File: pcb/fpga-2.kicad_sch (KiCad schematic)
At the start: 1 part, among them U5 XC7A100T-FGG484

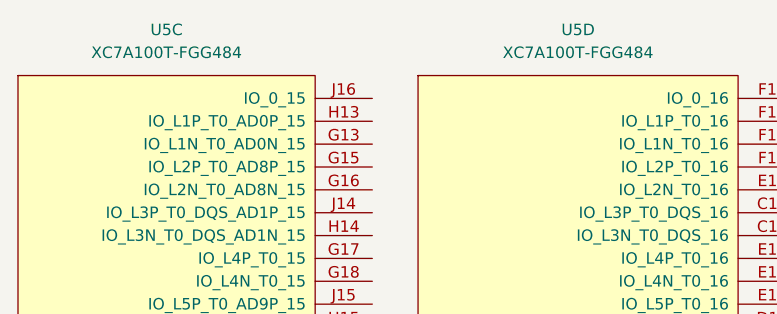
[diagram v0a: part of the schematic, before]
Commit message: moved stuff around, bom
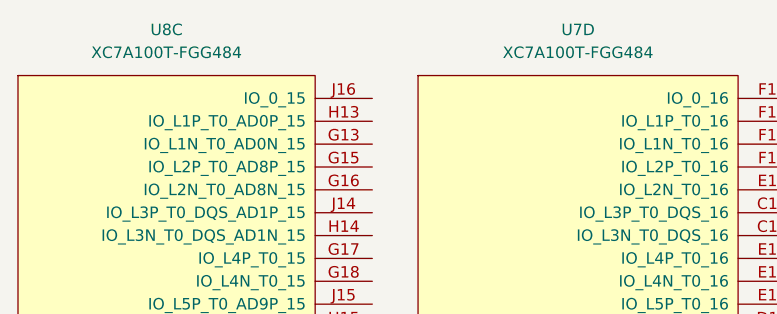
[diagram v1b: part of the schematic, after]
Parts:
- renumbered U5 to U7, U5 to U8
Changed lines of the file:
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@@
 		(dnp no)
 		(fields_autoplaced yes)
-		(property "Reference" "U5"
+		(property "Reference" "U7"
 			(at 99.06 25.4 0)
 			(effects
@@
 			(project "RPi-HwAB-1"
 				(path "/e63e39d7-6ac0-4ffd-8aa3-1841a4541b55/59d21473-a004-4514-8090-fd93db818925/ef42fd34-c1d8-421f-b8cb-1078e483aec9"
-					(reference "U5")
+					(reference "U7")
 					(unit 4)
 				)
@@
 		(dnp no)
 		(fields_autoplaced yes)
-		(property "Reference" "U5"
+		(property "Reference" "U8"
 			(at 53.34 25.4 0)
 			(effects
@@
 			(project "RPi-HwAB-1"
 				(path "/e63e39d7-6ac0-4ffd-8aa3-1841a4541b55/59d21473-a004-4514-8090-fd93db818925/ef42fd34-c1d8-421f-b8cb-1078e483aec9"
-					(reference "U5")
+					(reference "U8")
 					(unit 3)
 				)

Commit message: decoupling
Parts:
- added C129, C135, C136, C137, C138, C139, C140, C141, C142, C143, C144, C145: 0.1uF, Capacitor_SMD:C_0402_1005Metric, symbol library:C
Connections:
- net 3V3_FD: now reaches U7.A17 (VCCO_16)
- net 3V3_FD: now also U7.B14 (VCCO_16), U7.C21 (VCCO_16), U7.D18 (VCCO_16), U7.E15 (VCCO_16), U7.F22 (VCCO_16), U8.G19 (VCCO_15), U8.H16 (VCCO_15), U8.J13 (VCCO_15), U8.K20 (VCCO_15), U8.L17 (VCCO_15), U8.N21 (VCCO_15), C129.2, C135.2, C136.2, C137.2, C138.2, C139.2, C140.2, C141.2, C142.2, C143.2, C144.2, C145.2
- new net GND: C129.1, C135.1, C136.1, C137.1, C138.1, C139.1, C140.1, C141.1, C142.1, C143.1, C144.1, C145.1
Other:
- moved on the sheet: U7D, U8C

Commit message: bom
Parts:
- C30: renamed from C129; Part Description (none) -> CAP CER 0.1UF 16V X7R 0402
- C31: renamed from C140; Part Description (none) -> CAP CER 0.1UF 16V X7R 0402
- C32: renamed from C135; Part Description (none) -> CAP CER 0.1UF 16V X7R 0402
- C33: renamed from C141; Part Description (none) -> CAP CER 0.1UF 16V X7R 0402
- C34: renamed from C136; Part Description (none) -> CAP CER 0.1UF 16V X7R 0402
- C35: renamed from C142; Part Description (none) -> CAP CER 0.1UF 16V X7R 0402
- C36: renamed from C137; Part Description (none) -> CAP CER 0.1UF 16V X7R 0402
- C37: renamed from C143; Part Description (none) -> CAP CER 0.1UF 16V X7R 0402
- C38: renamed from C138; Part Description (none) -> CAP CER 0.1UF 16V X7R 0402
- C39: renamed from C144; Part Description (none) -> CAP CER 0.1UF 16V X7R 0402
- C40: renamed from C139; Part Description (none) -> CAP CER 0.1UF 16V X7R 0402
- C41: renamed from C145; Part Description (none) -> CAP CER 0.1UF 16V X7R 0402
- U7: Manufacturer (none) -> AMD; Manufacturer Product Number (none) -> XC7A100T-1FGG484C; Part Description (none) -> IC FPGA 285 I/O 484FBGA
- U7: renamed from U8; Manufacturer (none) -> AMD; Manufacturer Product Number (none) -> XC7A100T-1FGG484C; Part Description (none) -> IC FPGA 285 I/O 484FBGA
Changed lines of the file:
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@@
 		(on_board yes)
 		(dnp no)
-		(property "Reference" "C140"
+		(property "Reference" "C31"
 			(at 217.17 123.19 0)
 			(effects
@@
 			)
 		)
+		(property "Part Description" "CAP CER 0.1UF 16V X7R 0402"
+			(at 215.9 125.73 0)
+			(effects
+				(font
+					(size 1.27 1.27)
+				)
+				(hide yes)
+			)
+		)
 		(pin "1"
 		)
@@
 			(project "RPi-HwAB-1"
 				(path "/e63e39d7-6ac0-4ffd-8aa3-1841a4541b55/59d21473-a004-4514-8090-fd93db818925/ef42fd34-c1d8-421f-b8cb-1078e483aec9"
-					(reference "C140")
+					(reference "C31")
 					(unit 1)
 				)
@@
 			)
 		)
-		(property "Datasheet" ""
+		(property "Datasheet" "https://docs.amd.com/search/all?value-filters=Document_Type_custom~%2522Data+Sheet%2522_%2522Introductory+Resources%257CSelection+Guide%2522_%2522Introductory+Resources%257CWhite+Paper%2522*Product_custom~%2522Adaptive+SoCs+%2526+FPGAs%257CFPGA%257CArtix+7%2522&content-lang=en-US"
 			(at 144.78 76.2 0)
 			(effects
@@
 					(size 1.27 1.27)
 				)
+				(hide yes)
 			)
 		)
@@
 			)
 		)
+		(property "Manufacturer" "AMD"
+			(at 144.78 76.2 0)
+			(effects
+				(font
+					(size 1.27 1.27)
+				)
+				(hide yes)
+			)
+		)
+		(property "Manufacturer Product Number" "XC7A100T-1FGG484C"
+			(at 144.78 76.2 0)
+			(effects
+				(font
+					(size 1.27 1.27)
+				)
+				(hide yes)
+			)
+		)
+		(property "Part Description" "IC FPGA 285 I/O 484FBGA"
+			(at 144.78 76.2 0)
+			(effects
+				(font
+					(size 1.27 1.27)
+				)
+				(hide yes)
+			)
+		)
 		(pin "R19"
 		)
@@
 		(on_board yes)
 		(dnp no)
-		(property "Reference" "C137"
+		(property "Reference" "C36"
 			(at 240.03 97.79 0)
 			(effects
@@
 			)
 		)
+		(property "Part Description" "CAP CER 0.1UF 16V X7R 0402"
+			(at 238.76 100.33 0)
+			(effects
+				(font
+					(size 1.27 1.27)
+				)
+				(hide yes)
+			)
+		)
 		(pin "1"
 		)
@@
 			(project "RPi-HwAB-1"
 				(path "/e63e39d7-6ac0-4ffd-8aa3-1841a4541b55/59d21473-a004-4514-8090-fd93db818925/ef42fd34-c1d8-421f-b8cb-1078e483aec9"
-					(reference "C137")
+					(reference "C36")
 					(unit 1)
 				)
@@
 		(on_board yes)
 		(dnp no)
-		(property "Reference" "C141"
+		(property "Reference" "C33"
 			(at 224.79 123.19 0)
 			(effects
@@
 			)
 		)
+		(property "Part Description" "CAP CER 0.1UF 16V X7R 0402"
+			(at 223.52 125.73 0)
+			(effects
+				(font
+					(size 1.27 1.27)
+				)
+				(hide yes)
+			)
+		)
 		(pin "1"
 		)
@@
 			(project "RPi-HwAB-1"
 				(path "/e63e39d7-6ac0-4ffd-8aa3-1841a4541b55/59d21473-a004-4514-8090-fd93db818925/ef42fd34-c1d8-421f-b8cb-1078e483aec9"
-					(reference "C141")
+					(reference "C33")
 					(unit 1)
 				)
@@
 		(on_board yes)
 		(dnp no)
-		(property "Reference" "C138"
+		(property "Reference" "C38"
 			(at 247.65 97.79 0)
 			(effects
@@
 			)
 		)
+		(property "Part Description" "CAP CER 0.1UF 16V X7R 0402"
+			(at 246.38 100.33 0)
+			(effects
+				(font
+					(size 1.27 1.27)
+				)
+				(hide yes)
+			)
+		)
 		(pin "1"
 		)
@@
 			(project "RPi-HwAB-1"
 				(path "/e63e39d7-6ac0-4ffd-8aa3-1841a4541b55/59d21473-a004-4514-8090-fd93db818925/ef42fd34-c1d8-421f-b8cb-1078e483aec9"
-					(reference "C138")
+					(reference "C38")
 					(unit 1)
 				)
@@
 		(on_board yes)
 		(dnp no)
-		(property "Reference" "C129"
+		(property "Reference" "C30"
 			(at 217.17 97.79 0)
 			(effects
@@
 			)
 		)
+		(property "Part Description" "CAP CER 0.1UF 16V X7R 0402"
+			(at 215.9 100.33 0)
+			(effects
+				(font
+					(size 1.27 1.27)
+				)
+				(hide yes)
+			)
+		)
 		(pin "1"
 		)
@@
 			(project "RPi-HwAB-1"
 				(path "/e63e39d7-6ac0-4ffd-8aa3-1841a4541b55/59d21473-a004-4514-8090-fd93db818925/ef42fd34-c1d8-421f-b8cb-1078e483aec9"
-					(reference "C129")
+					(reference "C30")
 					(unit 1)
 				)
@@
 		(on_board yes)
 		(dnp no)
-		(property "Reference" "C142"
+		(property "Reference" "C35"
 			(at 232.41 123.19 0)
 			(effects
@@
 			)
 		)
+		(property "Part Description" "CAP CER 0.1UF 16V X7R 0402"
+			(at 231.14 125.73 0)
+			(effects
+				(font
+					(size 1.27 1.27)
+				)
+				(hide yes)
+			)
+		)
 		(pin "1"
 		)
@@
 			(project "RPi-HwAB-1"
 				(path "/e63e39d7-6ac0-4ffd-8aa3-1841a4541b55/59d21473-a004-4514-8090-fd93db818925/ef42fd34-c1d8-421f-b8cb-1078e483aec9"
-					(reference "C142")
+					(reference "C35")
 					(unit 1)
 				)
@@
 		(on_board yes)
 		(dnp no)
-		(property "Reference" "C144"
+		(property "Reference" "C39"
 			(at 247.65 123.19 0)
 			(effects
@@
 			)
 		)
+		(property "Part Description" "CAP CER 0.1UF 16V X7R 0402"
+			(at 246.38 125.73 0)
+			(effects
+				(font
+					(size 1.27 1.27)
+				)
+				(hide yes)
+			)
+		)
 		(pin "1"
 		)
@@
 			(project "RPi-HwAB-1"
 				(path "/e63e39d7-6ac0-4ffd-8aa3-1841a4541b55/59d21473-a004-4514-8090-fd93db818925/ef42fd34-c1d8-421f-b8cb-1078e483aec9"
-					(reference "C144")
+					(reference "C39")
 					(unit 1)
 				)
@@
 		(dnp no)
 		(fields_autoplaced yes)
-		(property "Reference" "#PWR058"
+		(property "Reference" "#PWR029"
 			(at 254 140.97 0)
 			(effects
@@
 			(project "RPi-HwAB-1"
 				(path "/e63e39d7-6ac0-4ffd-8aa3-1841a4541b55/59d21473-a004-4514-8090-fd93db818925/ef42fd34-c1d8-421f-b8cb-1078e483aec9"
-					(reference "#PWR058")
+					(reference "#PWR029")
 					(unit 1)
 				)
@@
 		(on_board yes)
 		(dnp no)
-		(property "Reference" "C143"
+		(property "Reference" "C37"
 			(at 240.03 123.19 0)
 			(effects
@@
 			)
 		)
+		(property "Part Description" "CAP CER 0.1UF 16V X7R 0402"
+			(at 238.76 125.73 0)
+			(effects
+				(font
+					(size 1.27 1.27)
+				)
+				(hide yes)
+			)
+		)
 		(pin "1"
 		)
@@
 			(project "RPi-HwAB-1"
 				(path "/e63e39d7-6ac0-4ffd-8aa3-1841a4541b55/59d21473-a004-4514-8090-fd93db818925/ef42fd34-c1d8-421f-b8cb-1078e483aec9"
-					(reference "C143")
+					(reference "C37")
 					(unit 1)
 				)
@@
 		(dnp no)
 		(fields_autoplaced yes)
-		(property "Reference" "U8"
+		(property "Reference" "U7"
 			(at 38.1 17.78 0)
 			(effects
@@
 			)
 		)
-		(property "Datasheet" ""
+		(property "Datasheet" "https://docs.amd.com/search/all?value-filters=Document_Type_custom~%2522Data+Sheet%2522_%2522Introductory+Resources%257CSelection+Guide%2522_%2522Introductory+Resources%257CWhite+Paper%2522*Product_custom~%2522Adaptive+SoCs+%2526+FPGAs%257CFPGA%257CArtix+7%2522&content-lang=en-US"
 			(at 38.1 76.2 0)
 			(effects
@@
 					(size 1.27 1.27)
 				)
+				(hide yes)
 			)
 		)
@@
 			)
 		)
+		(property "Manufacturer" "AMD"
+			(at 38.1 76.2 0)
+			(effects
+				(font
+					(size 1.27 1.27)
+				)
+				(hide yes)
+			)
+		)
+		(property "Manufacturer Product Number" "XC7A100T-1FGG484C"
+			(at 38.1 76.2 0)
+			(effects
+				(font
+					(size 1.27 1.27)
+				)
+				(hide yes)
+			)
+		)
+		(property "Part Description" "IC FPGA 285 I/O 484FBGA"
+			(at 38.1 76.2 0)
+			(effects
+				(font
+					(size 1.27 1.27)
+				)
+				(hide yes)
+			)
+		)
 		(pin "R19"
 		)
@@
 			(project "RPi-HwAB-1"
 				(path "/e63e39d7-6ac0-4ffd-8aa3-1841a4541b55/59d21473-a004-4514-8090-fd93db818925/ef42fd34-c1d8-421f-b8cb-1078e483aec9"
-					(reference "U8")
+					(reference "U7")
 					(unit 3)
 				)
@@
 		(on_board yes)
 		(dnp no)
-		(property "Reference" "C139"
+		(property "Reference" "C40"
 			(at 255.27 97.79 0)
 			(effects
@@
 			)
 		)
+		(property "Part Description" "CAP CER 0.1UF 16V X7R 0402"
+			(at 254 100.33 0)
+			(effects
+				(font
+					(size 1.27 1.27)
+				)
+				(hide yes)
+			)
+		)
 		(pin "1"
 		)
@@
 			(project "RPi-HwAB-1"
 				(path "/e63e39d7-6ac0-4ffd-8aa3-1841a4541b55/59d21473-a004-4514-8090-fd93db818925/ef42fd34-c1d8-421f-b8cb-1078e483aec9"
-					(reference "C139")
+					(reference "C40")
 					(unit 1)
 				)
@@
 		(on_board yes)
 		(dnp no)
-		(property "Reference" "C136"
+		(property "Reference" "C34"
 			(at 232.41 97.79 0)
 			(effects
@@
 			)
 		)
+		(property "Part Description" "CAP CER 0.1UF 16V X7R 0402"
+			(at 231.14 100.33 0)
+			(effects
+				(font
+					(size 1.27 1.27)
+				)
+				(hide yes)
+			)
+		)
 		(pin "1"
 		)
@@
 			(project "RPi-HwAB-1"
 				(path "/e63e39d7-6ac0-4ffd-8aa3-1841a4541b55/59d21473-a004-4514-8090-fd93db818925/ef42fd34-c1d8-421f-b8cb-1078e483aec9"
-					(reference "C136")
+					(reference "C34")
 					(unit 1)
 				)
@@
 		(dnp no)
 		(fields_autoplaced yes)
-		(property "Reference" "#PWR057"
+		(property "Reference" "#PWR028"
 			(at 254 115.57 0)
 			(effects
@@
 			(project "RPi-HwAB-1"
 				(path "/e63e39d7-6ac0-4ffd-8aa3-1841a4541b55/59d21473-a004-4514-8090-fd93db818925/ef42fd34-c1d8-421f-b8cb-1078e483aec9"
-					(reference "#PWR057")
+					(reference "#PWR028")
 					(unit 1)
 				)
@@
 		(on_board yes)
 		(dnp no)
-		(property "Reference" "C145"
+		(property "Reference" "C41"
 			(at 255.27 123.19 0)
 			(effects
@@
 			)
 		)
+		(property "Part Description" "CAP CER 0.1UF 16V X7R 0402"
+			(at 254 125.73 0)
+			(effects
+				(font
+					(size 1.27 1.27)
+				)
+				(hide yes)
+			)
+		)
 		(pin "1"
 		)
@@
 			(project "RPi-HwAB-1"
 				(path "/e63e39d7-6ac0-4ffd-8aa3-1841a4541b55/59d21473-a004-4514-8090-fd93db818925/ef42fd34-c1d8-421f-b8cb-1078e483aec9"
-					(reference "C145")
+					(reference "C41")
 					(unit 1)
 				)
@@
 		(on_board yes)
 		(dnp no)
-		(property "Reference" "C135"
+		(property "Reference" "C32"
 			(at 224.79 97.79 0)
 			(effects
@@
 			)
 		)
+		(property "Part Description" "CAP CER 0.1UF 16V X7R 0402"
+			(at 223.52 100.33 0)
+			(effects
+				(font
+					(size 1.27 1.27)
+				)
+				(hide yes)
+			)
+		)
 		(pin "1"
 		)
@@
 			(project "RPi-HwAB-1"
 				(path "/e63e39d7-6ac0-4ffd-8aa3-1841a4541b55/59d21473-a004-4514-8090-fd93db818925/ef42fd34-c1d8-421f-b8cb-1078e483aec9"
-					(reference "C135")
+					(reference "C32")
 					(unit 1)
 				)

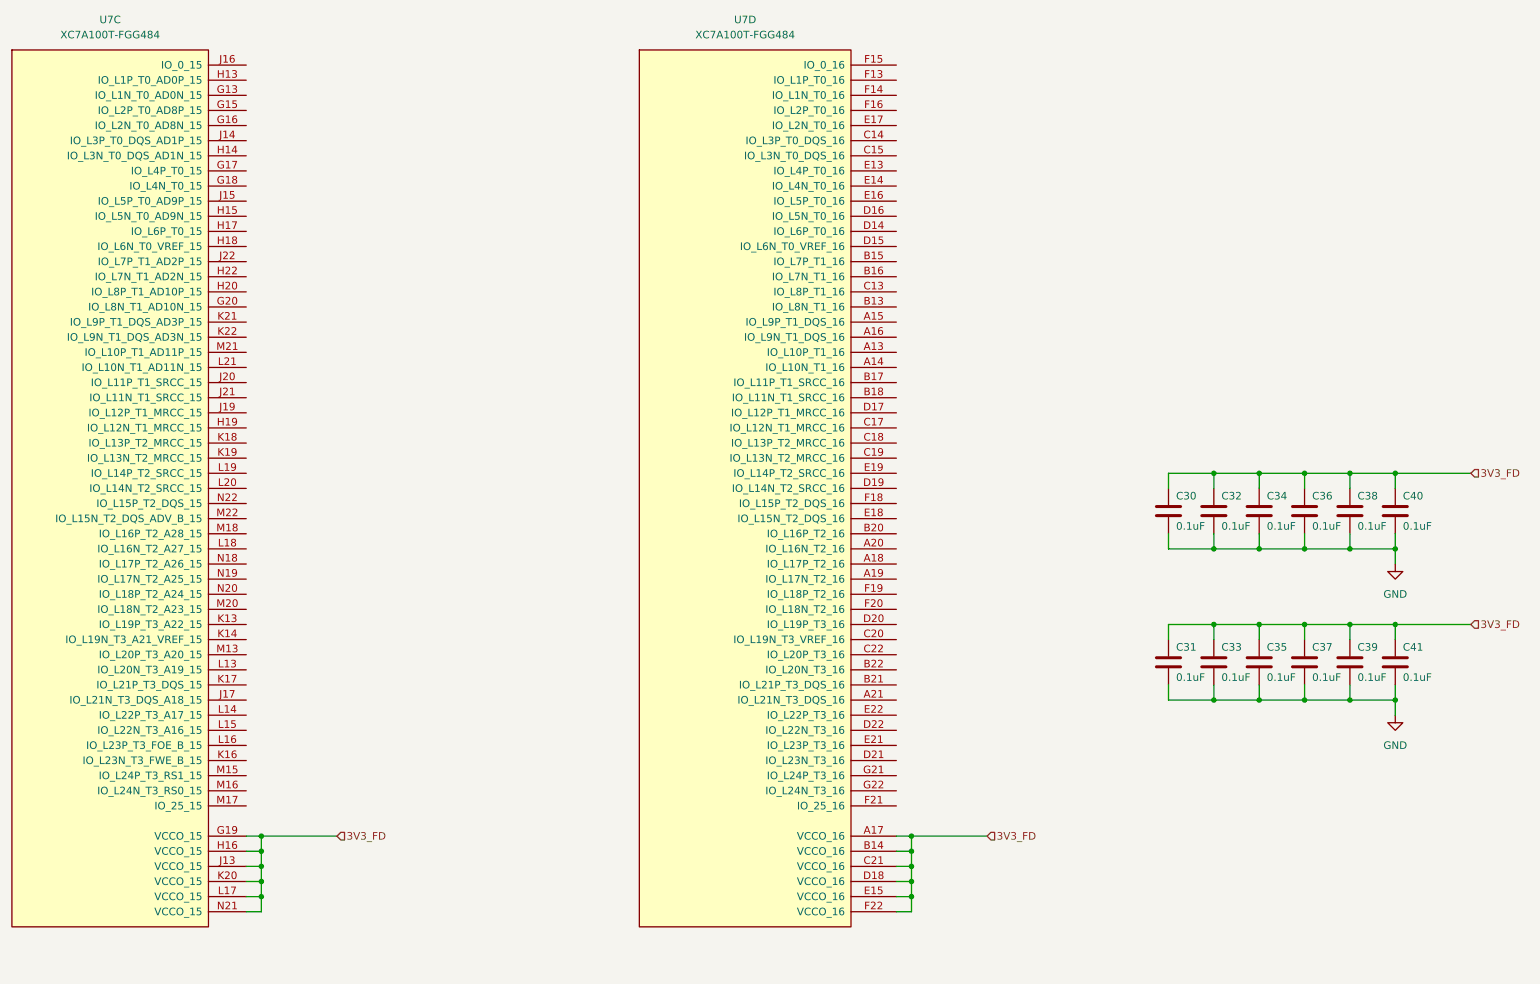
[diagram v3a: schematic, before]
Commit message: added mig ddr pinout constraints
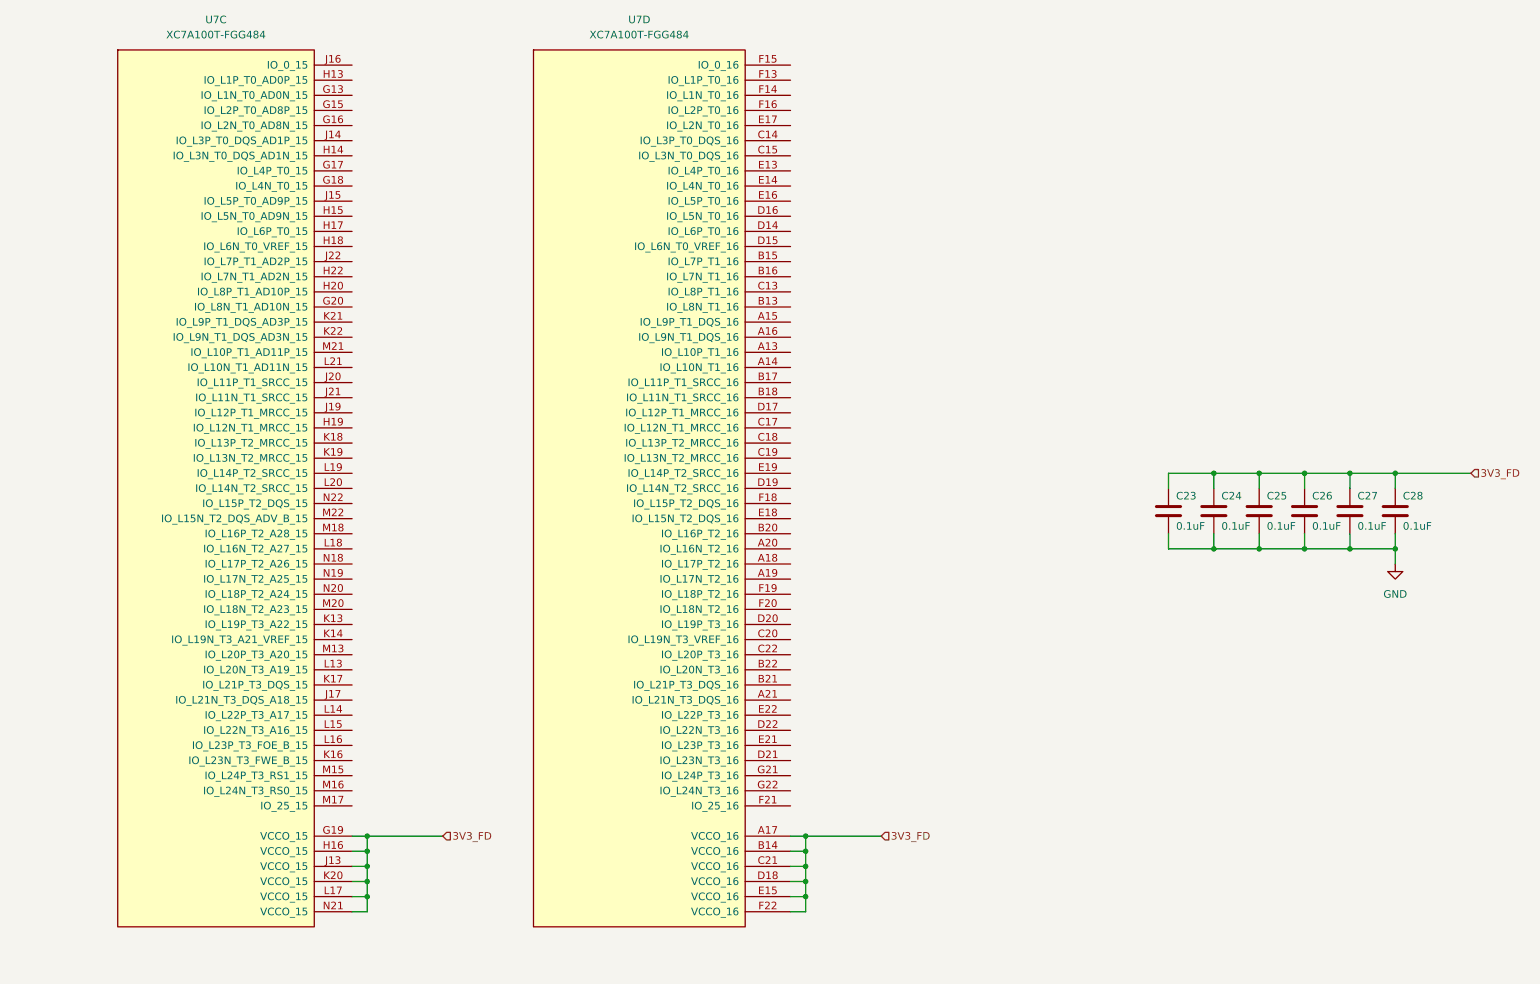
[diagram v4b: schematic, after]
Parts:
- removed C31, C33, C35, C37, C39, C41: 0.1uF, Capacitor_SMD:C_0402_1005Metric, symbol library:C
- renumbered C30 to C23, C32 to C24, C34 to C25, C36 to C26, C38 to C27, C40 to C28
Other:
- moved on the sheet: U7C, U7D
